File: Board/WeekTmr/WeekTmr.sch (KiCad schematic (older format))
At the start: 18 parts, among them J1 Screw_Terminal_01x03, J2 Screw_Terminal_01x03, J3 Barrel_Jack_MountingPin, J4 DS3231, K1 DIPxx-1Cxx-51x, K2 DIPxx-1Cxx-51x, Q1 BC817, Q2 BC817, SW1 DOWN_BUT, SW2 UP_BUT, SW3 SELECT_BUT, U1 NHD-0420H1Z

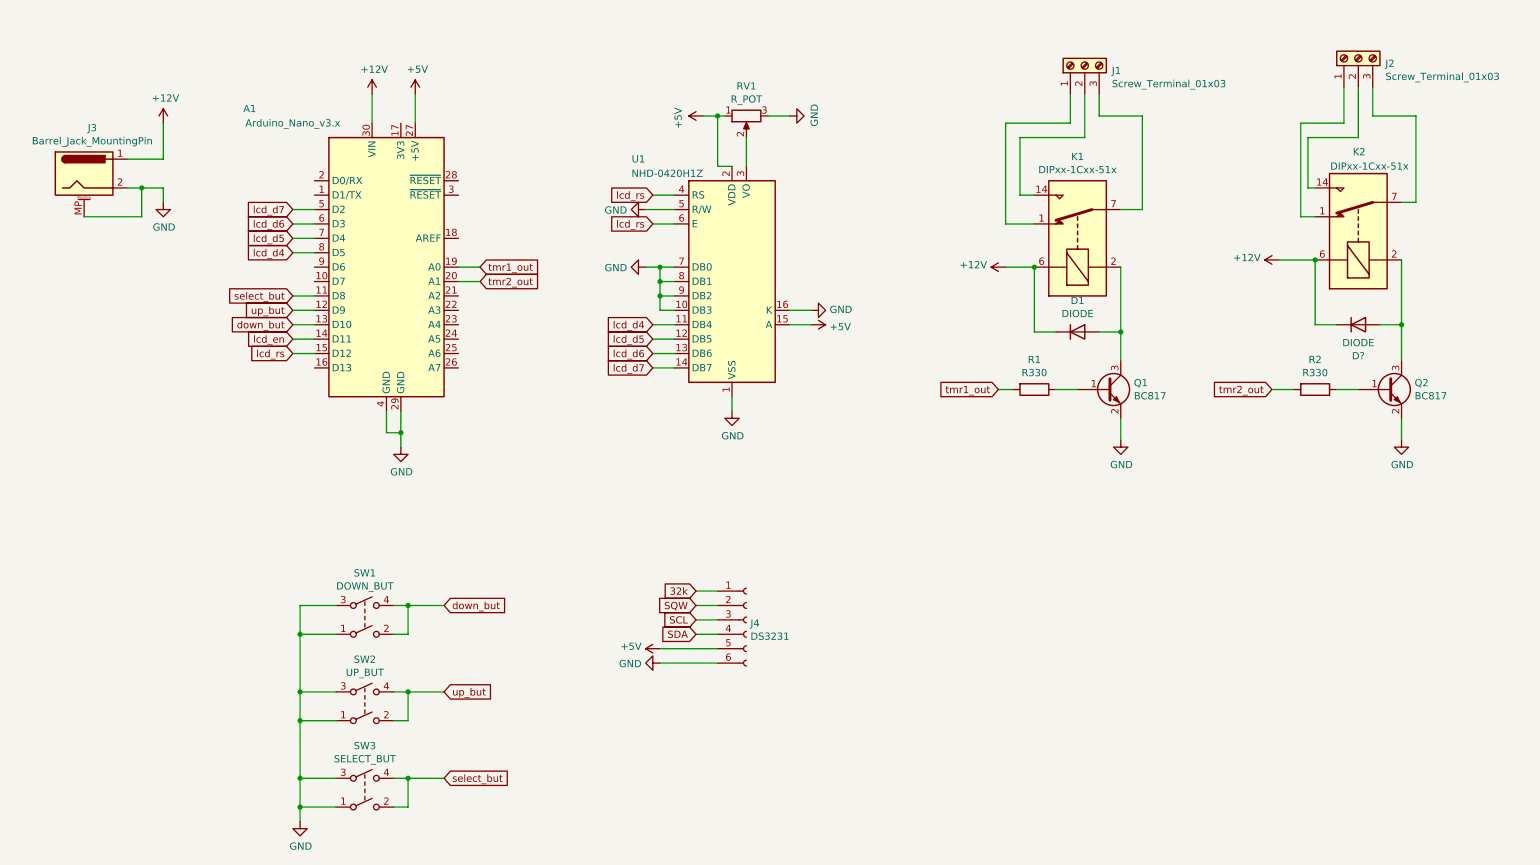
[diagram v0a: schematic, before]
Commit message: update schematic
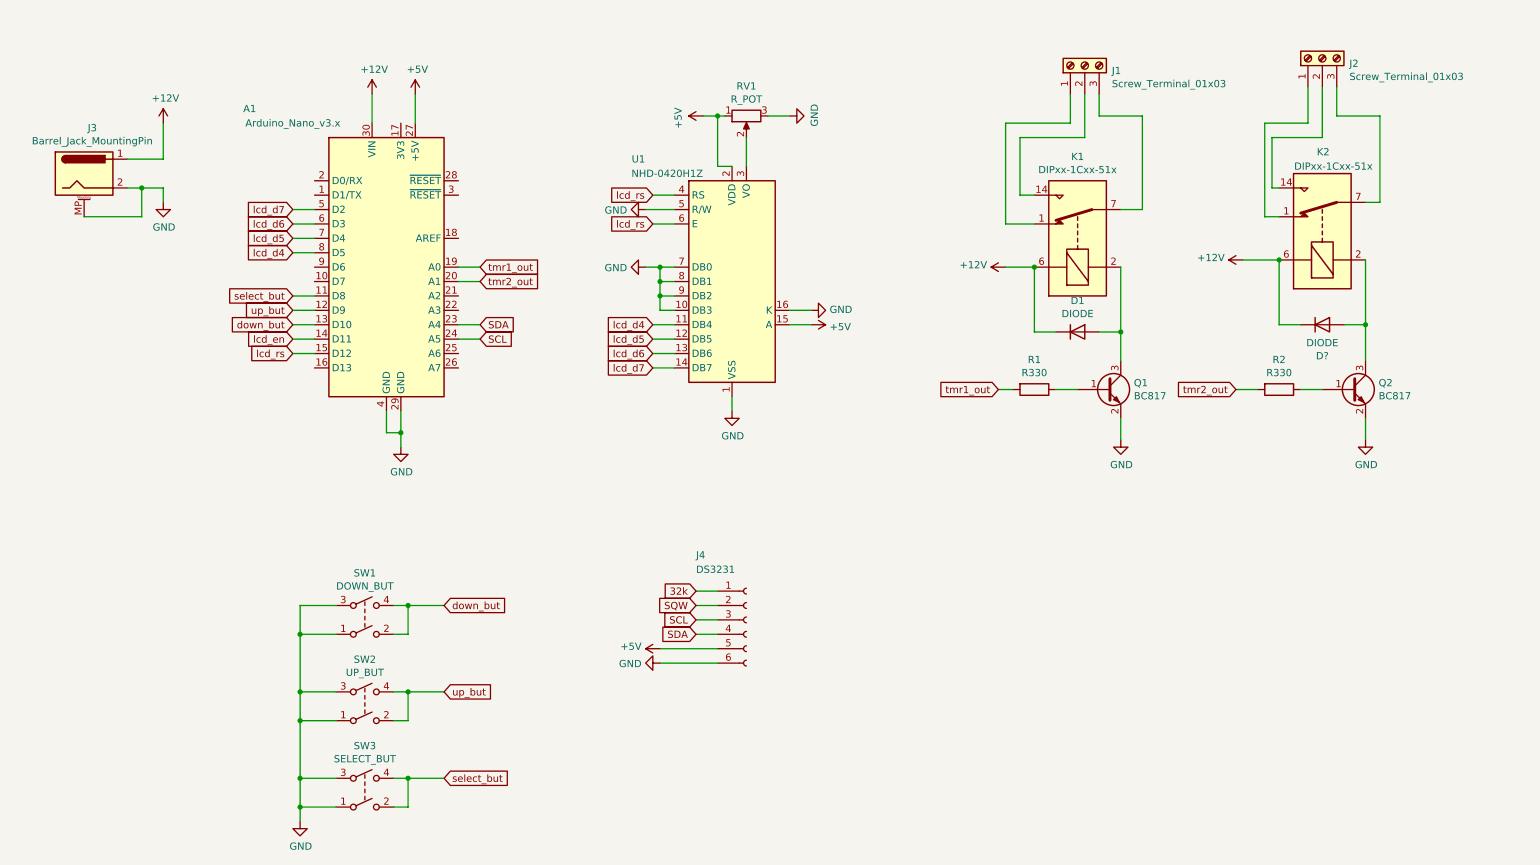
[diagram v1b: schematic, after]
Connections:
- net SCL: now also A1.24 (A5)
- net SDA: now also A1.23 (A4)
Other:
- moved on the sheet: D?, J2, K2, Q2, R2
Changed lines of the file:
@@
 L Simulation_SPICE:DIODE D?
 U 1 1 5F93350A
-P 10100 3000
-F 0 "D?" H 10100 3217 50  0000 C CNN
-F 1 "DIODE" H 10100 3126 50  0000 C CNN
-F 2 "" H 10100 3000 50  0001 C CNN
-F 3 "~" H 10100 3000 50  0001 C CNN
-F 4 "Y" H 10100 3000 50  0001 L CNN "Spice_Netlist_Enabled"
-F 5 "V" H 10100 3000 50  0001 L CNN "Spice_Primitive"
-	1    10100 3000
+P 9850 3000
+F 0 "D?" H 9850 3217 50  0000 C CNN
+F 1 "DIODE" H 9850 3126 50  0000 C CNN
+F 2 "" H 9850 3000 50  0001 C CNN
+F 3 "~" H 9850 3000 50  0001 C CNN
+F 4 "Y" H 9850 3000 50  0001 L CNN "Spice_Netlist_Enabled"
+F 5 "V" H 9850 3000 50  0001 L CNN "Spice_Primitive"
+	1    9850 3000
 	-1   0    0    1
 $EndComp
@@
 L Transistor_BJT:BC817 Q2
 U 1 1 5F943F2E
-P 10300 3450
-F 0 "Q2" H 10491 3496 50  0000 L CNN
-F 1 "BC817" H 10491 3405 50  0000 L CNN
-F 2 "Package_TO_SOT_SMD:SOT-23" H 10500 3375 50  0001 L CIN
-F 3 "http://www.fairchildsemi.com/ds/BC/BC817.pdf" H 10300 3450 50  0001 L CNN
-	1    10300 3450
+P 10050 3450
+F 0 "Q2" H 10241 3496 50  0000 L CNN
+F 1 "BC817" H 10241 3405 50  0000 L CNN
+F 2 "Package_TO_SOT_SMD:SOT-23" H 10250 3375 50  0001 L CIN
+F 3 "http://www.fairchildsemi.com/ds/BC/BC817.pdf" H 10050 3450 50  0001 L CNN
+	1    10050 3450
 	1    0    0    -1
 $EndComp
@@
 L Relay:DIPxx-1Cxx-51x K2
 U 1 1 5F931872
-P 10100 2350
-F 0 "K2" V 10650 2300 50  0000 L CNN
-F 1 "DIPxx-1Cxx-51x" V 10550 2000 50  0000 L CNN
-F 2 "Relay_THT:Relay_StandexMeder_DIP_LowProfile" H 10550 2300 50  0001 L CNN
-F 3 "https://standexelectronics.com/wp-content/uploads/datasheet_reed_relay_DIP.pdf" H 10100 2350 50  0001 C CNN
-	1    10100 2350
+P 9850 2350
+F 0 "K2" V 10400 2300 50  0000 L CNN
+F 1 "DIPxx-1Cxx-51x" V 10300 2000 50  0000 L CNN
+F 2 "Relay_THT:Relay_StandexMeder_DIP_LowProfile" H 10300 2300 50  0001 L CNN
+F 3 "https://standexelectronics.com/wp-content/uploads/datasheet_reed_relay_DIP.pdf" H 9850 2350 50  0001 C CNN
+	1    9850 2350
 	0    -1   -1   0
 $EndComp
@@
 L power:GND #PWR?
 U 1 1 5F948572
-P 10400 3800
-F 0 "#PWR?" H 10400 3550 50  0001 C CNN
-F 1 "GND" H 10405 3627 50  0000 C CNN
-F 2 "" H 10400 3800 50  0001 C CNN
-F 3 "" H 10400 3800 50  0001 C CNN
-	1    10400 3800
+P 10150 3800
+F 0 "#PWR?" H 10150 3550 50  0001 C CNN
+F 1 "GND" H 10155 3627 50  0000 C CNN
+F 2 "" H 10150 3800 50  0001 C CNN
+F 3 "" H 10150 3800 50  0001 C CNN
+	1    10150 3800
 	1    0    0    -1
 $EndComp
@@
 	8450 3650 8450 3800
 Wire Wire Line
-	10400 3650 10400 3800
+	10150 3650 10150 3800
 Wire Wire Line
 	8300 3050 8450 3050
@@
 	8450 3050 8450 3250
 Wire Wire Line
-	10250 3000 10400 3000
-Connection ~ 10400 3000
-Wire Wire Line
-	10400 3000 10400 3250
-Wire Wire Line
-	9950 3000 9800 3000
-Wire Wire Line
-	9800 3000 9800 2550
-Wire Wire Line
-	10400 2550 10400 3000
+	10000 3000 10150 3000
+Connection ~ 10150 3000
+Wire Wire Line
+	10150 3000 10150 3250
+Wire Wire Line
+	9700 3000 9550 3000
+Wire Wire Line
+	9550 3000 9550 2550
+Wire Wire Line
+	10150 2550 10150 3000
 Wire Wire Line
 	8450 2600 8450 3050
@@
 Text GLabel 7600 3450 0    50   Input ~ 0
 tmr1_out
-Text GLabel 9500 3450 0    50   Input ~ 0
+Text GLabel 9250 3450 0    50   Input ~ 0
 tmr2_out
 Wire Wire Line
-	9500 3450 9650 3450
+	9250 3450 9400 3450
 $Comp
 L power:+12V #PWR?
 U 1 1 5F97DBA8
-P 9550 2550
-F 0 "#PWR?" H 9550 2400 50  0001 C CNN
-F 1 "+12V" V 9565 2678 50  0000 L CNN
-F 2 "" H 9550 2550 50  0001 C CNN
-F 3 "" H 9550 2550 50  0001 C CNN
-	1    9550 2550
+P 9300 2550
+F 0 "#PWR?" H 9300 2400 50  0001 C CNN
+F 1 "+12V" V 9315 2678 50  0000 L CNN
+F 2 "" H 9300 2550 50  0001 C CNN
+F 3 "" H 9300 2550 50  0001 C CNN
+	1    9300 2550
 	0    -1   -1   0
 $EndComp
@@
 Connection ~ 7850 2600
 Wire Wire Line
-	9550 2550 9800 2550
-Connection ~ 9800 2550
+	9300 2550 9550 2550
+Connection ~ 9550 2550
 Wire Wire Line
 	2700 3100 2850 3100
@@
 	3250 1400 3250 1600
 Wire Wire Line
-	9950 3450 10100 3450
+	9700 3450 9850 3450
 $Comp
 L Device:R R2
 U 1 1 5F96E4A5
-P 9800 3450
-F 0 "R2" V 9593 3450 50  0000 C CNN
-F 1 "R330" V 9684 3450 50  0000 C CNN
-F 2 "" V 9730 3450 50  0001 C CNN
-F 3 "~" H 9800 3450 50  0001 C CNN
-	1    9800 3450
+P 9550 3450
+F 0 "R2" V 9343 3450 50  0000 C CNN
+F 1 "R330" V 9434 3450 50  0000 C CNN
+F 2 "" V 9480 3450 50  0001 C CNN
+F 3 "~" H 9550 3450 50  0001 C CNN
+	1    9550 3450
 	0    1    1    0
 $EndComp
@@
 L Connector:Screw_Terminal_01x03 J2
 U 1 1 5F9AD7D4
-P 10100 1150
-F 0 "J2" V 10064 962 50  0000 R CNN
-F 1 "Screw_Terminal_01x03" V 9973 962 50  0000 R CNN
-F 2 "" H 10100 1150 50  0001 C CNN
-F 3 "~" H 10100 1150 50  0001 C CNN
-	1    10100 1150
+P 9850 1150
+F 0 "J2" V 9814 962 50  0000 R CNN
+F 1 "Screw_Terminal_01x03" V 9723 962 50  0000 R CNN
+F 2 "" H 9850 1150 50  0001 C CNN
+F 3 "~" H 9850 1150 50  0001 C CNN
+	1    9850 1150
 	0    -1   -1   0
 $EndComp
@@
 	8100 1600 8100 1400
 Wire Wire Line
-	10200 1350 10200 1550
-Wire Wire Line
-	10200 1550 10500 1550
-Wire Wire Line
-	10500 1550 10500 2150
-Wire Wire Line
-	10500 2150 10400 2150
-Wire Wire Line
-	9800 2050 9750 2050
-Wire Wire Line
-	9750 2050 9750 1700
-Wire Wire Line
-	9750 1700 10100 1700
-Wire Wire Line
-	10100 1700 10100 1350
-Wire Wire Line
-	9800 2250 9700 2250
-Wire Wire Line
-	9700 2250 9700 1600
-Wire Wire Line
-	9700 1600 10000 1600
-Wire Wire Line
-	10000 1600 10000 1350
+	9950 1350 9950 1550
+Wire Wire Line
+	9950 1550 10250 1550
+Wire Wire Line
+	10250 1550 10250 2150
+Wire Wire Line
+	10250 2150 10150 2150
+Wire Wire Line
+	9550 2050 9500 2050
+Wire Wire Line
+	9500 2050 9500 1700
+Wire Wire Line
+	9500 1700 9850 1700
+Wire Wire Line
+	9850 1700 9850 1350
+Wire Wire Line
+	9550 2250 9450 2250
+Wire Wire Line
+	9450 2250 9450 1600
+Wire Wire Line
+	9450 1600 9750 1600
+Wire Wire Line
+	9750 1600 9750 1350
 $Comp
 L Connector:Conn_01x06_Female J4
 U 1 1 5F9C2C3A
 P 5850 5050
-F 0 "J4" H 5878 5026 50  0000 L CNN
-F 1 "DS3231" H 5878 4935 50  0000 L CNN
+F 0 "J4" H 5500 5500 50  0000 L CNN
+F 1 "DS3231" H 5500 5400 50  0000 L CNN
 F 2 "" H 5850 5050 50  0001 C CNN
 F 3 "~" H 5850 5050 50  0001 C CNN
@@
 Wire Wire Line
 	5250 5350 5650 5350
+Text GLabel 4000 3000 2    50   Input ~ 0
+SDA
+Text GLabel 4000 3100 2    50   Input ~ 0
+SCL
+Wire Wire Line
+	3850 3000 4000 3000
+Wire Wire Line
+	3850 3100 4000 3100
 $EndSCHEMATC

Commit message: pcb update
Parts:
- removed J1, J2: Screw_Terminal_01x03, symbol Connector:Screw_Terminal_01x03
- removed K1, K2: DIPxx-1Cxx-51x, Relay_THT:Relay_StandexMeder_DIP_LowProfile, symbol Relay:DIPxx-1Cxx-51x
- added D3, D4: LED, LED_THT:LED_D5.0mm_Clear, symbol Device:LED
- added J11: TMR1.1, TerminalBlock_Phoenix:TerminalBlock_Phoenix_MKDS-1,5-3-5.08_1x03_P5.08mm_Horizontal, symbol Connector:Screw_Terminal_01x03
- added J12: TMR1.2, TerminalBlock_Phoenix:TerminalBlock_Phoenix_MKDS-1,5-3-5.08_1x03_P5.08mm_Horizontal, symbol Connector:Screw_Terminal_01x03
- added J21: TMR2.1, TerminalBlock_Phoenix:TerminalBlock_Phoenix_MKDS-1,5-3-5.08_1x03_P5.08mm_Horizontal, symbol Connector:Screw_Terminal_01x03
- added J22: TMR2.2, TerminalBlock_Phoenix:TerminalBlock_Phoenix_MKDS-1,5-3-5.08_1x03_P5.08mm_Horizontal, symbol Connector:Screw_Terminal_01x03
- added K1, K2: FINDER-40.52, Relay_THT:Relay_DPDT_Finder_40.52, symbol Relay:FINDER-40.52
- added R3, R4: R620, Resistor_SMD:R_0805_2012Metric_Pad1.15x1.40mm_HandSolder, symbol Device:R
- D1: footprint (none) -> Diode_THT:D_DO-15_P15.24mm_Horizontal
- D2: renamed from D?; footprint (none) -> Diode_THT:D_DO-15_P15.24mm_Horizontal
- J3: footprint (none) -> KiCad_Library:BarrelJack_Horizontal_comet
- J4: footprint (none) -> KiCad_Library:DS3231_RTC_Module
- R1, R2: footprint (none) -> Resistor_SMD:R_0805_2012Metric_Pad1.15x1.40mm_HandSolder
- RV1: footprint (none) -> KiCad_Library:Pot_custom
- SW1, SW2, SW3: footprint (none) -> KiCad_Library:SW_Button
- U1: footprint Display:NHD-0420H1Z -> KiCad_Library:LCD_4x20_Stoian
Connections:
- net +12V: now also K1.A1, K2.A1, R3.1, R4.1
- net lcd_en: now also U1.6 (E)
- net lcd_rs: no longer U1.6 (E)
- net at D1.1 (A), Q1.3 (C): now also D3.1 (K), K1.A2
- net at D2.1 (A), Q2.3 (C): now also D4.1 (K), K2.A2
- new net: D3.2 (A), R3.2
- new net: D4.2 (A), R4.2
- new net COM1.1: J11.2 (Pin_2), K1.21
- new net COM1.2: J12.2 (Pin_2), K1.11
- new net COM2.1: J21.2 (Pin_2), K2.21
- new net COM2.2: J22.2 (Pin_2), K2.11
- new net NC1.1: J11.1 (Pin_1), K1.22
- new net NC1.2: J12.3 (Pin_3), K1.12
- new net NC2.1: J21.1 (Pin_1), K2.22
- new net NC2.2: J22.3 (Pin_3), K2.12
- new net NO1.1: J11.3 (Pin_3), K1.24
- new net NO1.2: J12.1 (Pin_1), K1.14
- new net NO2.1: J21.3 (Pin_3), K2.24
- new net NO2.2: J22.1 (Pin_1), K2.14
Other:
- moved on the sheet: D1, D2, Q1, Q2, R1, R2

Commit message: schem and board update
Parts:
- removed D1, D2: DIODE, Diode_THT:D_DO-15_P15.24mm_Horizontal, symbol Simulation_SPICE:DIODE
- added D1, D2: 1N5819, Diode_THT:D_DO-41_SOD81_P10.16mm_Horizontal, symbol Diode:1N5819
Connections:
- net +12V: now also D1.1 (K), D2.1 (K)
- net at D3.1 (K), K1.A2, Q1.3 (C): now also D1.2 (A)
- net at D4.1 (K), K2.A2, Q2.3 (C): now also D2.2 (A)
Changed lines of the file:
@@
-$EndComp
-$Comp
-L Simulation_SPICE:DIODE D1
-U 1 1 5F932D1D
-P 8100 4200
-F 0 "D1" H 8100 3983 50  0000 C CNN
-F 1 "DIODE" H 8100 4074 50  0000 C CNN
-F 2 "Diode_THT:D_DO-15_P15.24mm_Horizontal" H 8100 4200 50  0001 C CNN
-F 3 "~" H 8100 4200 50  0001 C CNN
-F 4 "Y" H 8100 4200 50  0001 L CNN "Spice_Netlist_Enabled"
-F 5 "V" H 8100 4200 50  0001 L CNN "Spice_Primitive"
-	1    8100 4200
-	-1   0    0    1
-$EndComp
-$Comp
-L Simulation_SPICE:DIODE D2
-U 1 1 5F93350A
-P 9800 4150
-F 0 "D2" H 9800 4367 50  0000 C CNN
-F 1 "DIODE" H 9800 4276 50  0000 C CNN
-F 2 "Diode_THT:D_DO-15_P15.24mm_Horizontal" H 9800 4150 50  0001 C CNN
-F 3 "~" H 9800 4150 50  0001 C CNN
-F 4 "Y" H 9800 4150 50  0001 L CNN "Spice_Netlist_Enabled"
-F 5 "V" H 9800 4150 50  0001 L CNN "Spice_Primitive"
-	1    9800 4150
-	-1   0    0    1
 $EndComp
 $Comp
@@
 	10100 5250 10100 5400
 Wire Wire Line
-	8250 4200 8400 4200
-Wire Wire Line
-	9950 4150 10100 4150
-Wire Wire Line
 	10100 4600 10100 4850
 Wire Wire Line
-	9650 4150 9500 4150
-Wire Wire Line
 	8400 3750 8400 4200
-Wire Wire Line
-	7950 4200 7800 4200
 Wire Wire Line
 	7800 4200 7800 3750
@@
 Wire Wire Line
 	9650 4600 10100 4600
-Wire Wire Line
-	10100 4150 10100 4600
 Connection ~ 10100 4600
 $Comp
@@
 	0    -1   -1   0
 $EndComp
-Wire Wire Line
-	10100 3750 10100 4150
-Connection ~ 10100 4150
 Wire Wire Line
 	9500 4150 9500 3750
@@
 Wire Wire Line
 	8250 1850 8400 1850
+$Comp
+L Diode:1N5819 D2
+U 1 1 5F96FCC2
+P 9850 4250
+F 0 "D2" H 9850 4466 50  0000 C CNN
+F 1 "1N5819" H 9850 4375 50  0000 C CNN
+F 2 "Diode_THT:D_DO-41_SOD81_P10.16mm_Horizontal" H 9850 4075 50  0001 C CNN
+F 3 "http://www.vishay.com/docs/88525/1n5817.pdf" H 9850 4250 50  0001 C CNN
+	1    9850 4250
+	1    0    0    -1
+$EndComp
+$Comp
+L Diode:1N5819 D1
+U 1 1 5F97069A
+P 8000 4200
+F 0 "D1" H 8000 4416 50  0000 C CNN
+F 1 "1N5819" H 8000 4325 50  0000 C CNN
+F 2 "Diode_THT:D_DO-41_SOD81_P10.16mm_Horizontal" H 8000 4025 50  0001 C CNN
+F 3 "http://www.vishay.com/docs/88525/1n5817.pdf" H 8000 4200 50  0001 C CNN
+	1    8000 4200
+	1    0    0    -1
+$EndComp
+Wire Wire Line
+	7800 4200 7850 4200
+Wire Wire Line
+	8150 4200 8400 4200
+Wire Wire Line
+	10100 3750 10100 4250
+Wire Wire Line
+	9500 4150 9600 4150
+Wire Wire Line
+	9600 4150 9600 4250
+Wire Wire Line
+	9600 4250 9700 4250
+Wire Wire Line
+	10000 4250 10100 4250
+Connection ~ 10100 4250
+Wire Wire Line
+	10100 4250 10100 4600
 $EndSCHEMATC

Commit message: board update
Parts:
- A1: footprint Module:Arduino_Nano -> KiCad_Library:Arduino_Nano_direct_Slot
- J11, J12, J21, J22: footprint TerminalBlock_Phoenix:TerminalBlock_Phoenix_MKDS-1,5-3-5.08_1x03_P5.08mm_Horizontal -> KiCad_Library:COMET_2EDGR-5.08-14-00AH
- R1, R2: footprint Resistor_SMD:R_0805_2012Metric_Pad1.15x1.40mm_HandSolder -> Resistor_THT:R_Axial_DIN0207_L6.3mm_D2.5mm_P15.24mm_Horizontal
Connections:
- net NC1.1: now also J11.3 (Pin_3); no longer J11.1 (Pin_1)
- net NC1.2: now also J12.1 (Pin_1); no longer J12.3 (Pin_3)
- net NC2.1: now also J21.3 (Pin_3); no longer J21.1 (Pin_1)
- net NC2.2: now also J22.1 (Pin_1); no longer J22.3 (Pin_3)
- net NO1.1: now also J11.1 (Pin_1); no longer J11.3 (Pin_3)
- net NO1.2: now also J12.3 (Pin_3); no longer J12.1 (Pin_1)
- net NO2.1: now also J21.1 (Pin_1); no longer J21.3 (Pin_3)
- net NO2.2: now also J22.3 (Pin_3); no longer J22.1 (Pin_1)
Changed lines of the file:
@@
 F 0 "A1" H 2400 3700 50  0000 C CNN
 F 1 "Arduino_Nano_v3.x" H 2700 3600 50  0000 C CNN
-F 2 "Module:Arduino_Nano" H 3350 2600 50  0001 C CIN
+F 2 "KiCad_Library:Arduino_Nano_direct_Slot" H 3350 2600 50  0001 C CIN
 F 3 "http://www.mouser.com/pdfdocs/Gravitech_Arduino_Nano3_0.pdf" H 3350 2600 50  0001 C CNN
 	1    3350 2600
@@
 F 0 "R1" V 7593 5050 50  0000 C CNN
 F 1 "R330" V 7684 5050 50  0000 C CNN
-F 2 "Resistor_SMD:R_0805_2012Metric_Pad1.15x1.40mm_HandSolder" V 7730 5050 50  0001 C CNN
+F 2 "Resistor_THT:R_Axial_DIN0207_L6.3mm_D2.5mm_P15.24mm_Horizontal" V 7730 5050 50  0001 C CNN
 F 3 "~" H 7800 5050 50  0001 C CNN
 	1    7800 5050
@@
 F 0 "R2" V 9293 5050 50  0000 C CNN
 F 1 "R330" V 9384 5050 50  0000 C CNN
-F 2 "Resistor_SMD:R_0805_2012Metric_Pad1.15x1.40mm_HandSolder" V 9430 5050 50  0001 C CNN
+F 2 "Resistor_THT:R_Axial_DIN0207_L6.3mm_D2.5mm_P15.24mm_Horizontal" V 9430 5050 50  0001 C CNN
 F 3 "~" H 9500 5050 50  0001 C CNN
 	1    9500 5050
@@
 F 0 "J21" H 9368 875 50  0000 C CNN
 F 1 "TMR2.1" H 9368 966 50  0000 C CNN
-F 2 "TerminalBlock_Phoenix:TerminalBlock_Phoenix_MKDS-1,5-3-5.08_1x03_P5.08mm_Horizontal" H 9450 1200 50  0001 C CNN
+F 2 "KiCad_Library:COMET_2EDGR-5.08-14-00AH" H 9450 1200 50  0001 C CNN
 F 3 "~" H 9450 1200 50  0001 C CNN
 	1    9450 1200
@@
 F 0 "J22" H 9368 1425 50  0000 C CNN
 F 1 "TMR2.2" H 9368 1516 50  0000 C CNN
-F 2 "TerminalBlock_Phoenix:TerminalBlock_Phoenix_MKDS-1,5-3-5.08_1x03_P5.08mm_Horizontal" H 9450 1750 50  0001 C CNN
+F 2 "KiCad_Library:COMET_2EDGR-5.08-14-00AH" H 9450 1750 50  0001 C CNN
 F 3 "~" H 9450 1750 50  0001 C CNN
 	1    9450 1750
@@
 F 0 "J11" H 7968 875 50  0000 C CNN
 F 1 "TMR1.1" H 7968 966 50  0000 C CNN
-F 2 "TerminalBlock_Phoenix:TerminalBlock_Phoenix_MKDS-1,5-3-5.08_1x03_P5.08mm_Horizontal" H 8050 1200 50  0001 C CNN
+F 2 "KiCad_Library:COMET_2EDGR-5.08-14-00AH" H 8050 1200 50  0001 C CNN
 F 3 "~" H 8050 1200 50  0001 C CNN
 	1    8050 1200
@@
 F 0 "J12" H 7968 1425 50  0000 C CNN
 F 1 "TMR1.2" H 7968 1516 50  0000 C CNN
-F 2 "TerminalBlock_Phoenix:TerminalBlock_Phoenix_MKDS-1,5-3-5.08_1x03_P5.08mm_Horizontal" H 8050 1750 50  0001 C CNN
+F 2 "KiCad_Library:COMET_2EDGR-5.08-14-00AH" H 8050 1750 50  0001 C CNN
 F 3 "~" H 8050 1750 50  0001 C CNN
 	1    8050 1750
@@
 Text GLabel 9800 1750 2    50   Input ~ 0
 COM2.2
+Text GLabel 8400 1300 2    50   Input ~ 0
+NO1.1
 Text GLabel 8400 1100 2    50   Input ~ 0
-NO1.1
-Text GLabel 8400 1300 2    50   Input ~ 0
 NC1.1
 Wire Wire Line
-	8250 1300 8400 1300
-Wire Wire Line
 	8250 1200 8400 1200
-Wire Wire Line
-	8250 1100 8400 1100
+Text GLabel 8400 1650 2    50   Input ~ 0
+NO1.2
 Text GLabel 8400 1850 2    50   Input ~ 0
-NO1.2
-Text GLabel 8400 1650 2    50   Input ~ 0
 NC1.2
+Text GLabel 9800 1300 2    50   Input ~ 0
+NO2.1
 Text GLabel 9800 1100 2    50   Input ~ 0
-NO2.1
-Text GLabel 9800 1300 2    50   Input ~ 0
 NC2.1
 Wire Wire Line
-	9650 1100 9800 1100
-Wire Wire Line
 	9650 1200 9800 1200
-Wire Wire Line
-	9650 1300 9800 1300
+Text GLabel 9800 1650 2    50   Input ~ 0
+NO2.2
 Text GLabel 9800 1850 2    50   Input ~ 0
-NO2.2
-Text GLabel 9800 1650 2    50   Input ~ 0
 NC2.2
 Wire Wire Line
-	9650 1650 9800 1650
-Wire Wire Line
 	9650 1750 9800 1750
 Wire Wire Line
-	9650 1850 9800 1850
-Wire Wire Line
-	8250 1650 8400 1650
-Wire Wire Line
 	8250 1750 8400 1750
-Wire Wire Line
-	8250 1850 8400 1850
 $Comp
 L Diode:1N5819 D2
@@
 Wire Wire Line
 	10100 4250 10100 4600
+Wire Wire Line
+	8250 1100 8400 1100
+Wire Wire Line
+	8250 1300 8400 1300
+Wire Wire Line
+	8250 1650 8400 1650
+Wire Wire Line
+	8250 1850 8400 1850
+Wire Wire Line
+	9650 1100 9800 1100
+Wire Wire Line
+	9650 1300 9800 1300
+Wire Wire Line
+	9650 1650 9800 1650
+Wire Wire Line
+	9650 1850 9800 1850
 $EndSCHEMATC
